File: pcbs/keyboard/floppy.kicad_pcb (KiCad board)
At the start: 2 copper layers, 94 x 90 mm, 44 parts, among them SW1 Choc, U1 ProMicro

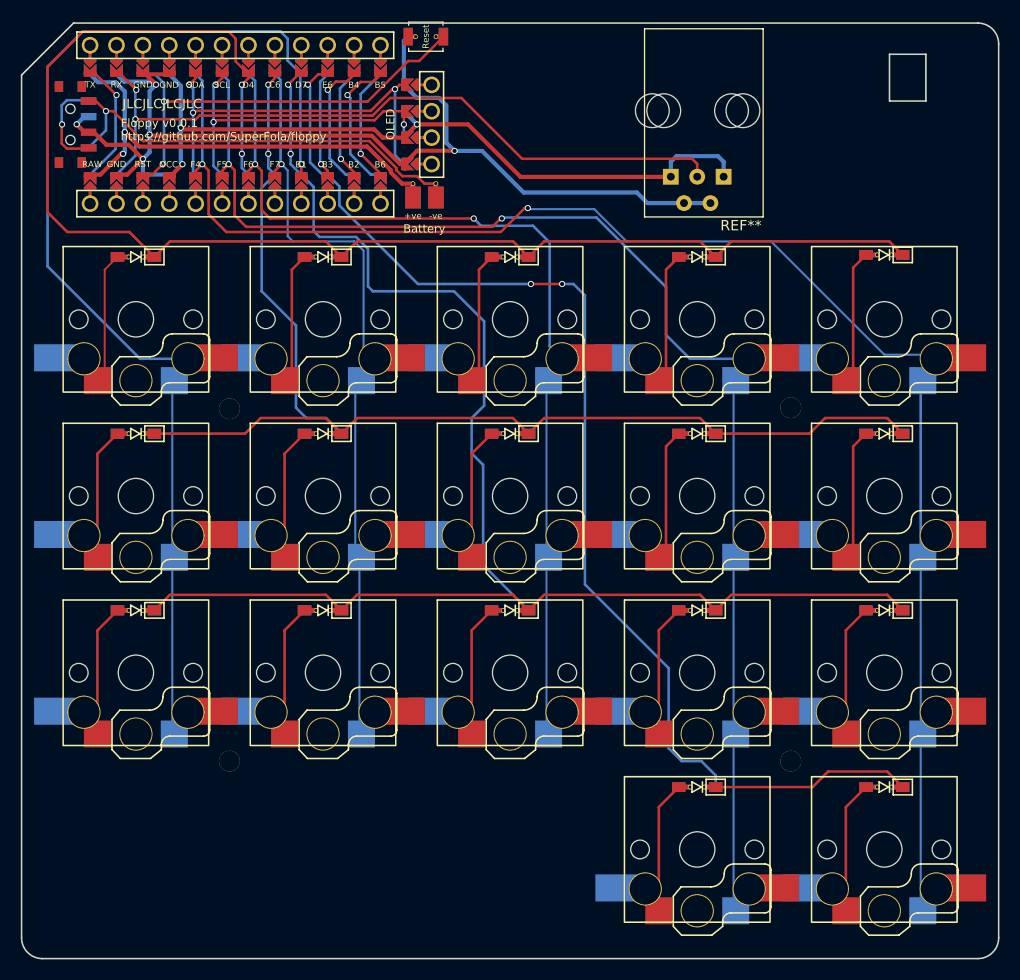
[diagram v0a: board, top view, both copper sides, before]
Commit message: feat: moving the pinky column downward, adding backplate
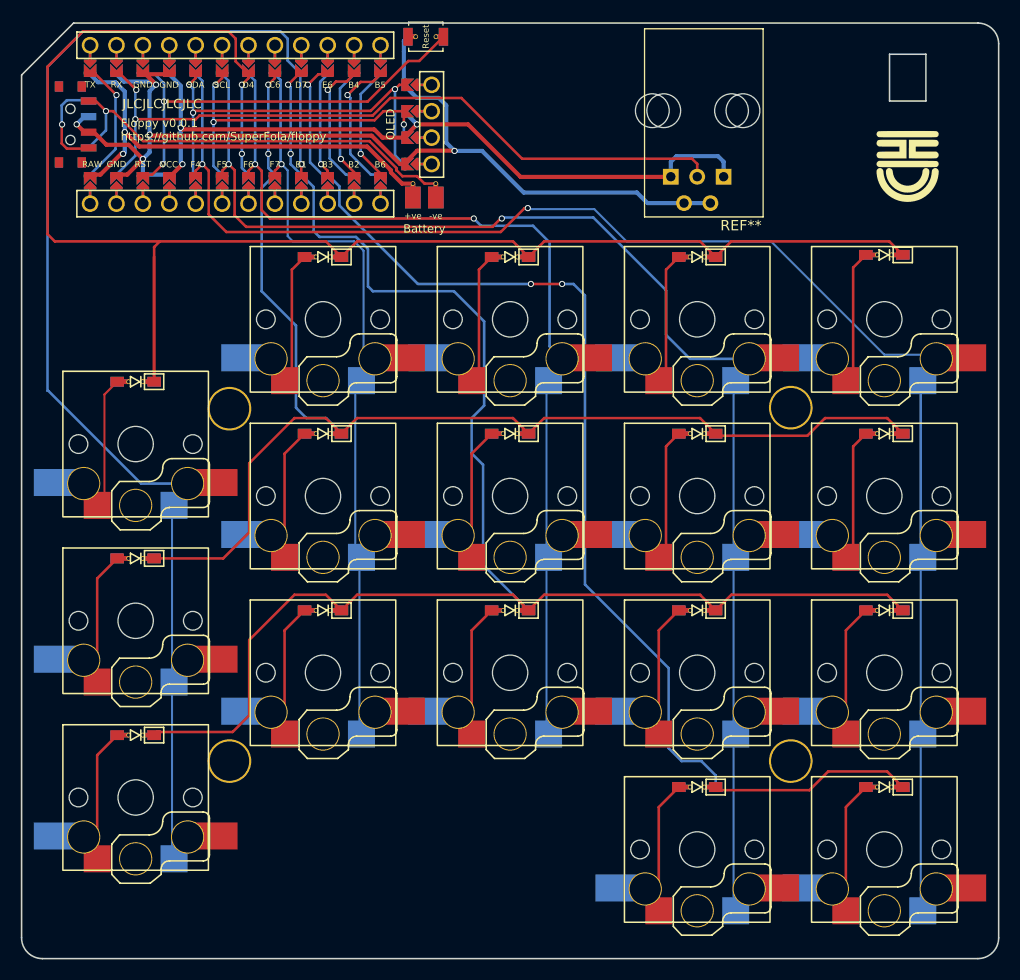
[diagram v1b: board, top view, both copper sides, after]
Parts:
- added G***: LOGO, LOGO, F.Cu at (189.8, 55.0)
- added G***: LOGO, LOGO, B.Cu at (189.8, 55.0)
- REF** (x4): value M2_2mm_hole -> h2; footprint floppy:M2_2mm_hole -> floppy:M2_hole_4.2mm
- moved D13 12.0 mm to (115.5, 109.7)
- moved D13 12.0 mm to (115.5, 75.7)
- moved D13 12.0 mm to (115.5, 92.7)
- moved SW1 12.0 mm to (115.5, 98.7)
- moved SW1 12.0 mm to (115.5, 115.7)
- moved SW1 12.0 mm to (115.5, 81.7)
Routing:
- net row0: track 136.9 -> 162.6 mm
- net col0: track 109.5 -> 120.0 mm
- net row2: track 146.4 -> 155.7 mm
- net row1: track 116.9 -> 125.9 mm
- net Net-(D1-A): track 12.7 -> 11.7 mm
